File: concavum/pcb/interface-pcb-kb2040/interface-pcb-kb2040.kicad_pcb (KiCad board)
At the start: 2 copper layers, 36 x 42 mm, 11 parts, among them J1 Audio_Jack, J2 FPC_connector, U1 Adafruit_KB2040, U2 MCP23017_SO

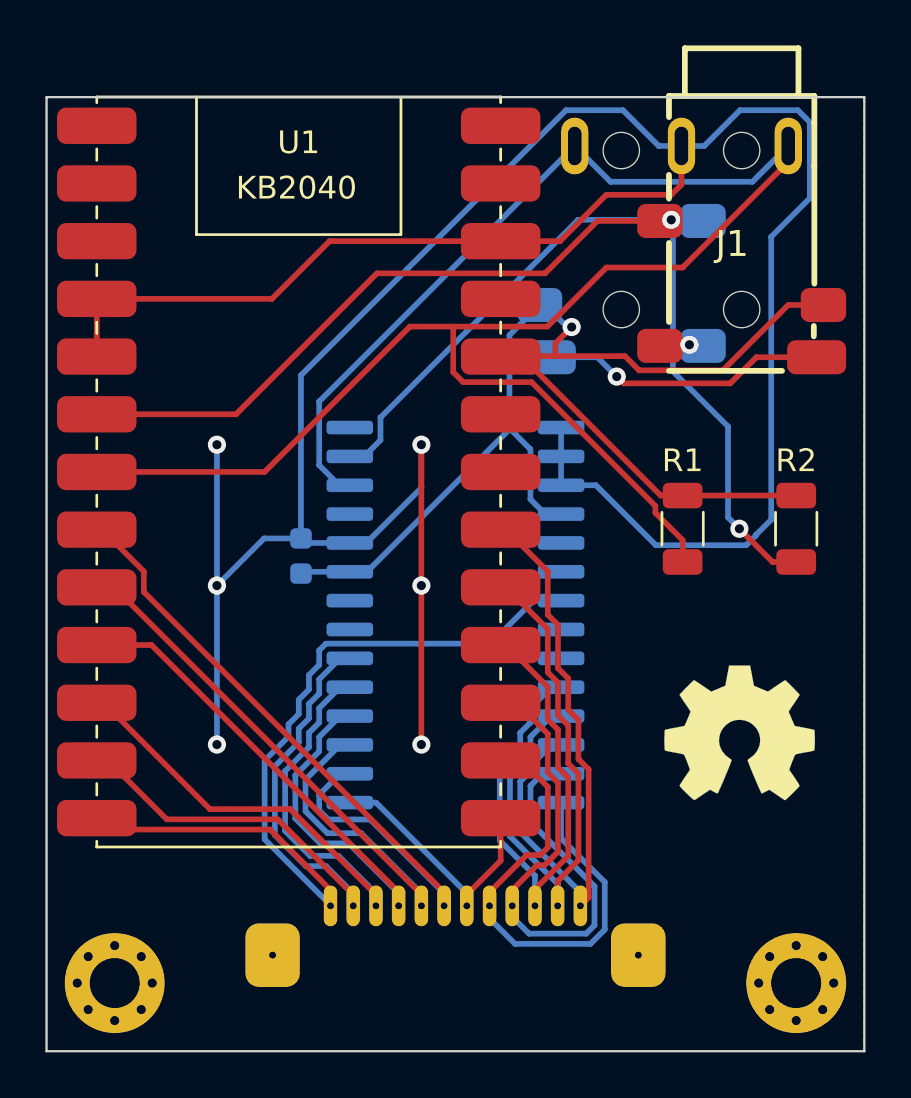
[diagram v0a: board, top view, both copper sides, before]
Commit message: Replace elongated holes with ordinary ones
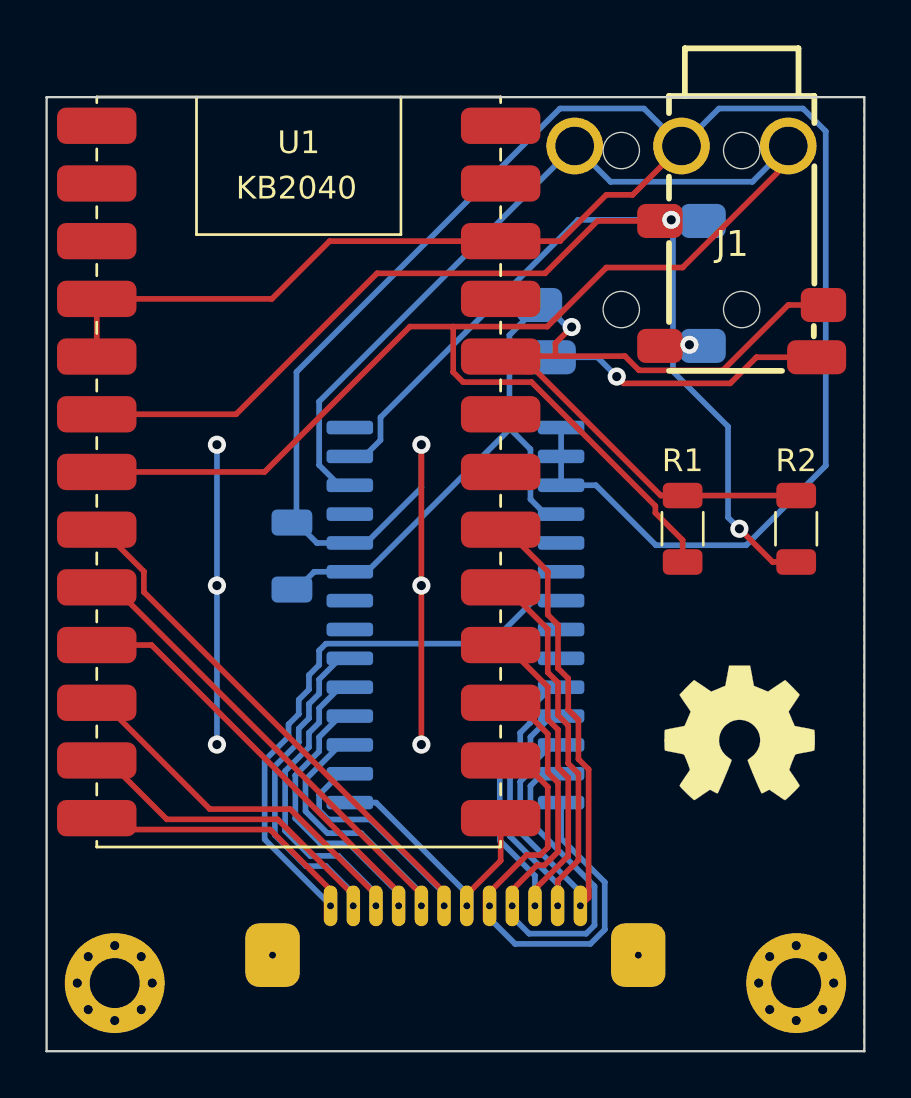
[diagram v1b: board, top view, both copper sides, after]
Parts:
- C1: footprint Capacitor_SMD:C_0603_1608Metric -> Capacitor_SMD:C_1206_3216Metric
- moved C1 0.40 mm to (143.8, 96.2)
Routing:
- net GND: track 139.2 -> 134.6 mm

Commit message: Add option to use MCP23018 instead of MCP23017
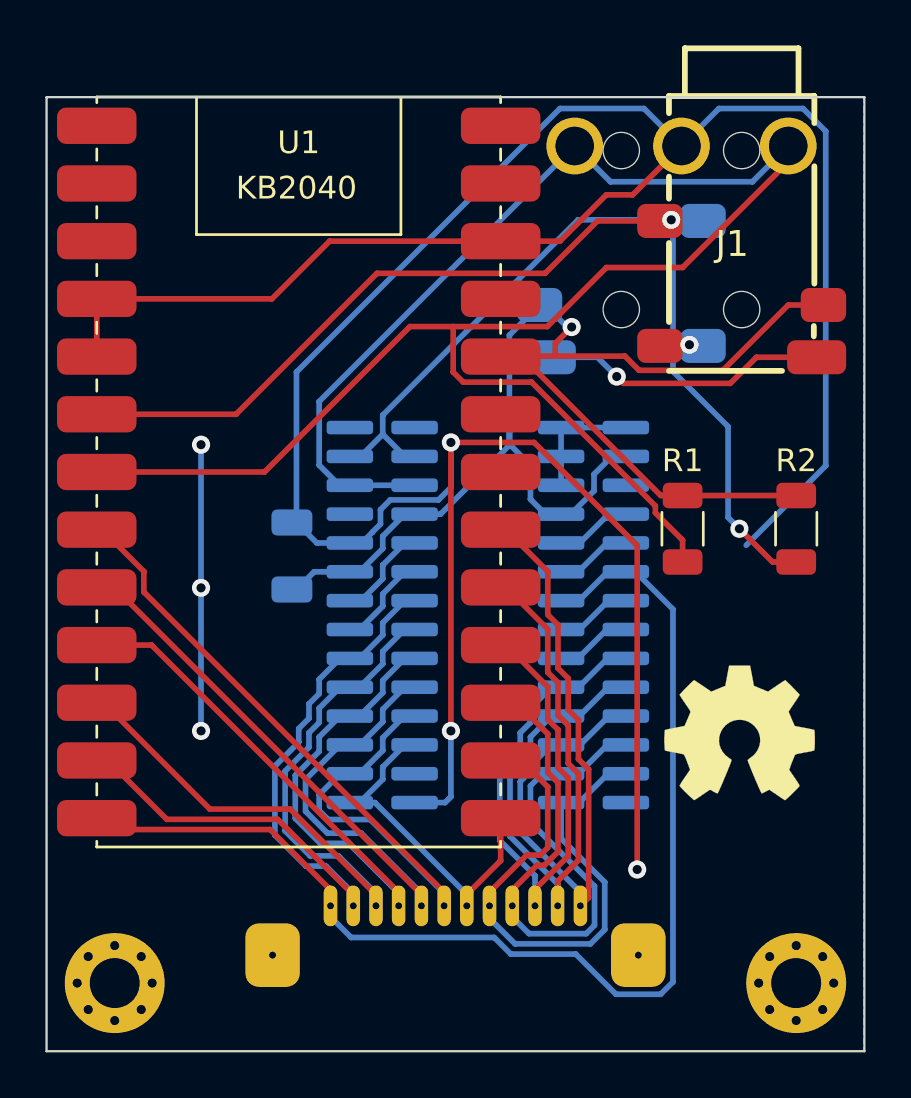
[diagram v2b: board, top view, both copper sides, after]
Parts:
- U2: value MCP23017_SO -> MCP23017/MCP23018; footprint Package_SO:SOIC-28W_7.5x17.9mm_P1.27mm -> Custom:MCP23017_SO_MCP23018_SO
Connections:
- U2 pad 16: GND -> unconnected-(U2-Pad16)
- U2 pad 17: GND -> unconnected-(U2-Pad17)
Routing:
- net GND: track 134.6 -> 158.6 mm
- net /ROW1: track 37.9 -> 52.6 mm
- net +3V3: track 60.0 -> 65.8 mm
- net unconnected-(U2-Pad8): track 0.00 -> 4.25 mm
- net /COL5: track 33.6 -> 37.8 mm
- net /COL4: track 31.5 -> 35.7 mm
- net /COL2: track 29.7 -> 33.9 mm
- net /COL3: track 30.6 -> 34.8 mm
- net unconnected-(U2-Pad7): track 0.00 -> 4.22 mm
- net /COL1: track 28.7 -> 32.9 mm
- net /COL6: track 11.8 -> 16.0 mm
- net /ROW5: track 26.4 -> 29.7 mm
- net /ROW2: track 21.9 -> 25.3 mm
- net unconnected-(U2-Pad23): track 0.00 -> 3.38 mm
- net /ROW6: track 27.6 -> 31.0 mm
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
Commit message: Change FPC connector pinout to increase clearances
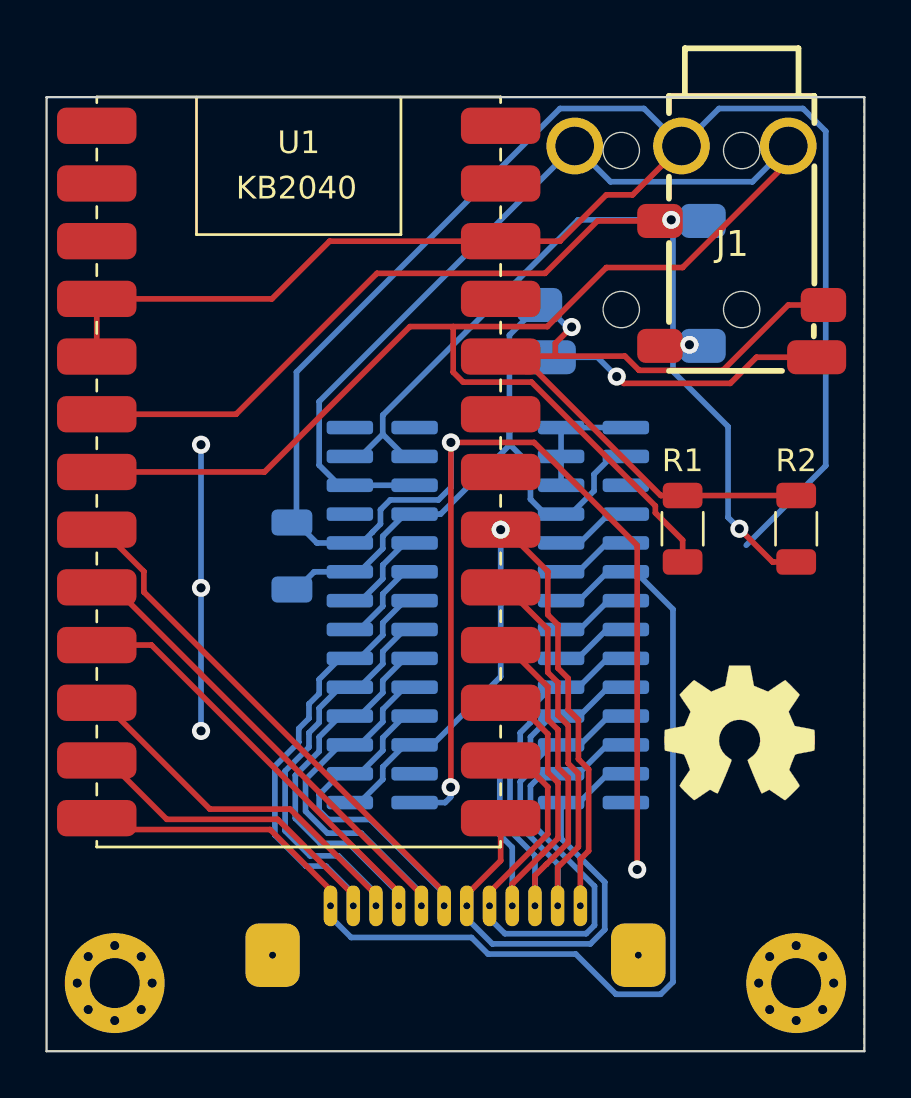
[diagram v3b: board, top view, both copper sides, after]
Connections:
- J2 pad 10: /ROW4 -> /ROW5
- J2 pad 11: /ROW5 -> /ROW6
- J2 pad 12: /ROW6 -> /COL6
- J2 pad 7: /COL6 -> /ROW2
- J2 pad 8: /ROW2 -> /ROW3
- J2 pad 9: /ROW3 -> /ROW4
- U1 pad 14: /COL6 -> /ROW2
- U1 pad 15: /ROW2 -> /ROW3
- U1 pad 16: /ROW3 -> /ROW4
- U1 pad 17: /ROW4 -> /ROW5
- U1 pad 18: /ROW5 -> /ROW6
- U1 pad 19: /ROW6 -> /COL6
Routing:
- net /COL6: track 16.0 -> 34.2 mm, vias 0 -> 1
- net /ROW2: track 25.3 -> 21.6 mm
- net /ROW6: track 31.0 -> 28.1 mm
- net /ROW5: track 29.7 -> 26.8 mm
- net /ROW4: track 28.5 -> 25.8 mm
- net +3V3: track 65.8 -> 64.1 mm
- net /ROW3: track 28.2 -> 26.7 mm
- net /SDA: track 69.9 -> 69.1 mm
- net /ROW1: track 52.6 -> 52.0 mm
